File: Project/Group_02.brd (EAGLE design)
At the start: 68.6 x 40.6 mm, 29 parts, among them J1 POWER_JACKPTH_LOCK, U1 +12v

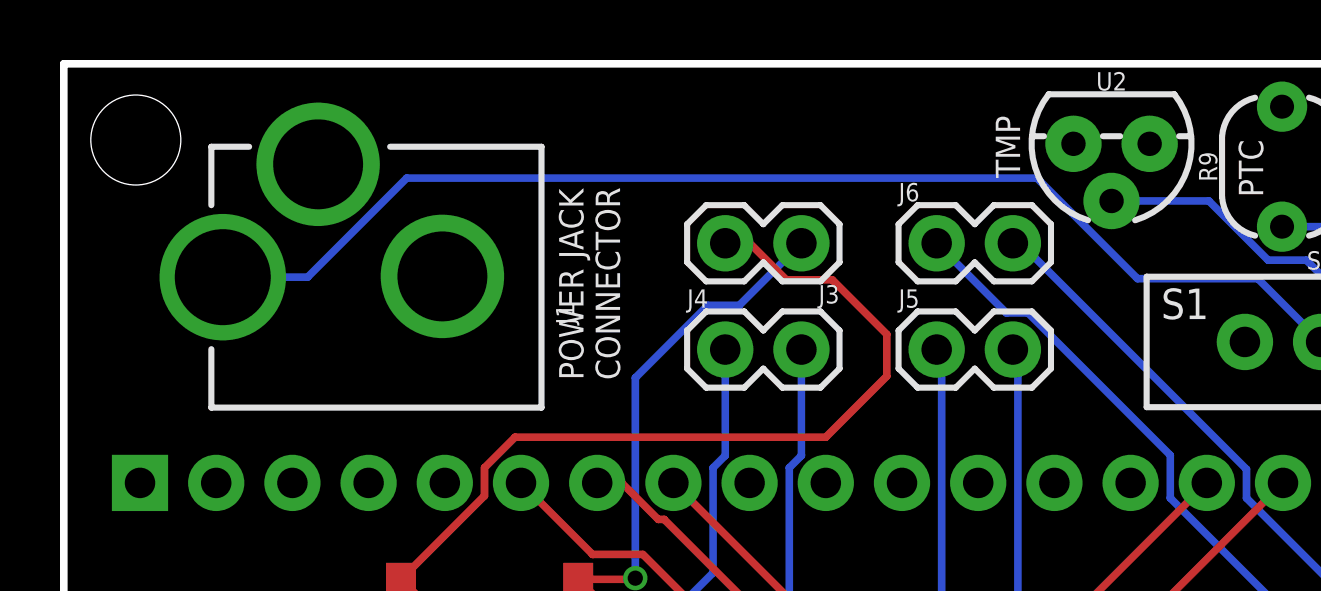
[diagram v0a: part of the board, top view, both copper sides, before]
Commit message: rotazione power jack
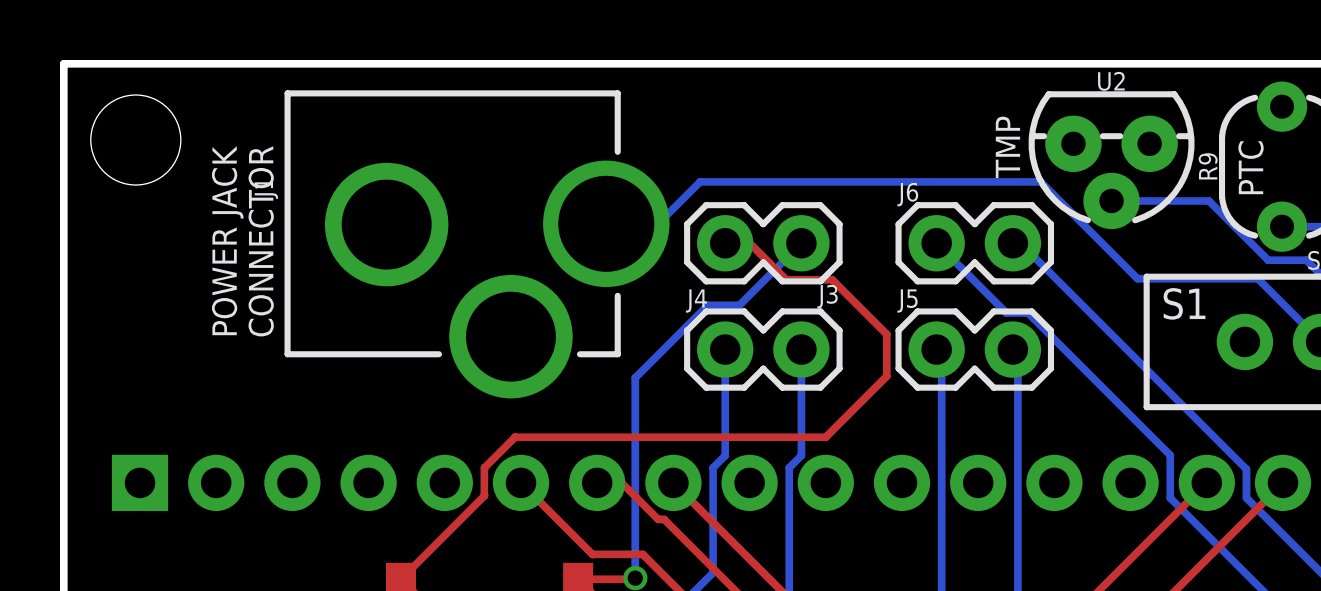
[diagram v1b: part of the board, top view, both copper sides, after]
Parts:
- moved J1 15.1 mm to (4.21, 35.3), turned to 270 degrees
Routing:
- net N$1: track 40.2 -> 26.6 mm
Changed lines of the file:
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@@
 <text x="66.675" y="27.94" size="0.8128" layer="22" rot="MR0">5V</text>
 <text x="64.897" y="27.94" size="0.8128" layer="22" rot="MR0">GND</text>
-<text x="18.542" y="30.099" size="0.8128" layer="21" rot="R90">POWER JACK
+<text x="6.985" y="31.496" size="0.8128" layer="21" rot="R90">POWER JACK
 CONNECTOR</text>
 <text x="56.261" y="11.557" size="1.016" layer="21">V REG</text>
@@
 <attribute name="VALUE" x="60.325" y="2.9845" size="0.6096" layer="27" font="vector" ratio="20" rot="R180" align="top-center"/>
 </element>
-<element name="J1" library="SparkFun-Connectors" package="POWER_JACK_PTH_LOCK" value="POWER_JACKPTH_LOCK" x="19.177" y="33.528" smashed="yes" rot="R90">
-<attribute name="NAME" x="17.018" y="31.9532" size="0.6096" layer="25" font="vector" ratio="20" rot="R90"/>
-<attribute name="PROD_ID" value="CONN-08197" x="47.117" y="53.848" size="1.778" layer="27" rot="R90" display="off"/>
-<attribute name="SF_ID" value="PRT-00119" x="47.117" y="53.848" size="1.778" layer="27" rot="R90" display="off"/>
-<attribute name="VALUE" x="18.034" y="31.623" size="0.6096" layer="27" font="vector" ratio="20" rot="R90"/>
+<element name="J1" library="SparkFun-Connectors" package="POWER_JACK_PTH_LOCK" value="POWER_JACKPTH_LOCK" x="4.205" y="35.306" smashed="yes" rot="R270">
+<attribute name="NAME" x="6.364" y="36.8808" size="0.6096" layer="25" font="vector" ratio="20" rot="R270"/>
+<attribute name="PROD_ID" value="CONN-08197" x="-23.735" y="14.986" size="1.778" layer="27" rot="R270" display="off"/>
+<attribute name="SF_ID" value="PRT-00119" x="-23.735" y="14.986" size="1.778" layer="27" rot="R270" display="off"/>
+<attribute name="VALUE" x="5.348" y="37.211" size="0.6096" layer="27" font="vector" ratio="20" rot="R270"/>
 </element>
 <element name="J2" library="SparkFun-Connectors" package="1X02" value="" x="63.627" y="31.115" smashed="yes">
@@
 <contactref element="J1" pad="PWR"/>
 <contactref element="S1" pad="2"/>
-<wire x1="5.2992" y1="33.528" x2="8.128" y2="33.528" width="0.254" layer="16"/>
-<wire x1="8.128" y1="33.528" x2="11.43" y2="36.83" width="0.254" layer="16"/>
+<wire x1="21.209" y1="36.703" x2="19.812" y2="35.306" width="0.254" layer="16"/>
+<wire x1="18.0828" y1="35.306" x2="19.812" y2="35.306" width="0.254" layer="16"/>
 <wire x1="39.8018" y1="33.4772" x2="41.91" y2="31.369" width="0.254" layer="16"/>
-<wire x1="32.4387875" y1="36.83" x2="35.7915875" y2="33.4772" width="0.254" layer="16"/>
-<wire x1="11.43" y1="36.83" x2="32.4387875" y2="36.83" width="0.254" layer="16"/>
+<wire x1="32.5657875" y1="36.703" x2="35.7915875" y2="33.4772" width="0.254" layer="16"/>
+<wire x1="21.209" y1="36.703" x2="32.5657875" y2="36.703" width="0.254" layer="16"/>
 <wire x1="35.7915875" y1="33.4772" x2="39.8018" y2="33.4772" width="0.254" layer="16"/>
 </signal>
